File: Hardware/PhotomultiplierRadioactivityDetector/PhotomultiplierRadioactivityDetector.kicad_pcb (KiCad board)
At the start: 2 copper layers, 100 x 100 mm, 83 parts, among them J1 Conn_01x04, J10 Conn_01x01_Male, J11 Conn_01x01_Male, J12 Conn_01x01_Male, J13 Conn_01x01_Male, J14 Conn_01x01_Male, J2 Conn_02x05_Counter_Clockwise, J3 Conn_01x01_Male, J4 Conn_01x01_Male, J5 Conn_01x01_Male, J6 Conn_01x01_Male, J7 Conn_01x01_Male, J8 Conn_01x01_Male, J9 Conn_01x01_Male, Q1 2N7002, Q2 Q_NPN_BEC, U1 Opamp_Dual_Generic, U2 MCP3425A0T-ECH, U3 MCP3425A0T-ECH, U4 STM8S003F3P

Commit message: initial version rework
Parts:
- removed RV1: R_POT_TRIM, Potentiometer_THT:Potentiometer_Bourns_3296W_Vertical
- added D6: 1n148, Diode_SMD:D_MiniMELF, F.Cu at (87.9, 181.0)
- added D7: red, LED_SMD:LED_0805_2012Metric, F.Cu at (111.7, 156.4)
- added J15: Conn_01x02_Female, Connector_PinHeader_2.54mm:PinHeader_2x01_P2.54mm_Vertical, F.Cu at (116.0, 186.0)
- added R31: 2k2, Resistor_SMD:R_0805_2012Metric_Pad1.15x1.40mm_HandSolder, F.Cu at (96.6, 161.8)
- added R32: 510R, Resistor_SMD:R_0805_2012Metric_Pad1.15x1.40mm_HandSolder, F.Cu at (91.9, 162.1)
- added R33: 510R, Resistor_SMD:R_0805_2012Metric_Pad1.15x1.40mm_HandSolder, F.Cu at (87.1, 162.1)
- added R34: 510R, Resistor_SMD:R_0805_2012Metric_Pad1.15x1.40mm_HandSolder, F.Cu at (93.5, 158.8)
- added R35: 10k, Resistor_SMD:R_0805_2012Metric_Pad1.15x1.40mm_HandSolder, F.Cu at (40.0, 173.8)
- added R36: 10k, Resistor_SMD:R_0805_2012Metric_Pad1.15x1.40mm_HandSolder, F.Cu at (44.8, 170.9)
- added Rel1: RSM850B-6112-85-1005, Relay_THT:Relay_DPDT_Omron_G6K-2P-Y, F.Cu at (86.4, 169.8)
- C1, C6, C9: value 100n -> 10n
- C10, C11, C12, C13, C14, C15, C16, C17, C18, C19, C20, C21: value C -> 10n/3kV
- C2: value 10u -> 10n; footprint Capacitor_Tantalum_SMD:CP_EIA-3528-21_Kemet-B -> Capacitor_SMD:C_0805_2012Metric_Pad1.15x1.40mm_HandSolder
- C7: value 10n -> 680n
- C8: value 680n -> 100n
- D2: value yellow -> 1n148; footprint LED_SMD:LED_0805_2012Metric -> Diode_SMD:D_MiniMELF
- D3: value 0R resistor -> yellow; footprint Diode_SMD:D_MiniMELF -> LED_SMD:LED_0805_2012Metric
- D4: value green -> 0R resistor; footprint LED_SMD:LED_0805_2012Metric -> Diode_SMD:D_MiniMELF
- D5: value red -> green
- Q2: footprint Package_TO_SOT_SMD:SOT-323_SC-70_Handsoldering -> Package_TO_SOT_SMD:SOT-323_SC-70
- R10: value 2k2 -> 1k
- R11: value 2k2 -> 10k
- R12, R13: value 510R -> 0R
- R14: value 510R -> 2k2
- R15, R16, R17, R18, R19, R20, R22, R23, R24, R25, R26, R27, R28, R29, R30: value R -> 150k
- R2, R7: value 0R -> 10k
- R3: value 27k -> 10k
- R4, R5, R8, R9: value 1k -> 10k
- R6: value 0R -> 100R
- U1: value Opamp_Dual_Generic -> TL074; footprint Package_SO:SOIC-8_3.9x4.9mm_P1.27mm -> Package_SO:SOIC-14_3.9x8.7mm_P1.27mm
- U2: value MCP3425A0T-ECH -> STM8S003F3P; footprint Package_TO_SOT_SMD:SOT-23-6_Handsoldering -> Package_SO:TSSOP-20_4.4x6.5mm_P0.65mm
- U4: value STM8S003F3P -> TL074; footprint Package_SO:TSSOP-20_4.4x6.5mm_P0.65mm -> Package_SO:SOIC-14_3.9x8.7mm_P1.27mm
- moved J1 76.7 mm to (111.7, 144.9)
- moved R21 71.1 mm to (95.0, 115.0)
- moved J11 69.9 mm to (93.0, 95.0)
- moved R14 68.5 mm to (116.4, 144.1)
- moved R24 64.2 mm to (90.0, 120.0)
- moved TP2 64.2 mm to (120.3, 150.1)
- moved R26 63.2 mm to (100.0, 130.0)
- moved TP4 61.1 mm to (120.0, 153.2)
- moved J3 59.8 mm to (37.0, 95.0)
- moved C6 58.3 mm to (116.4, 147.1)
- moved D3 57.7 mm to (116.3, 153.0)
- moved C2 57.6 mm to (101.8, 169.1)
- moved J2 57.4 mm to (98.3, 144.9)
- moved C7 56.4 mm to (116.4, 150.0)
- moved R25 54.9 mm to (85.0, 110.0)
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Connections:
- C1 pad 1: ANODE_OUTPUT -> Net-(C1-Pad1)
- C2 pad 1: VCC_5V -> ANODE_OUTPUT
- C2 pad 2: ANODE_OUTPUT -> Net-(C2-Pad2)
- C6 pad 2: VCC_5V -> /DataProcessing/RST
- C7 pad 2: /DataAcquisition/RST -> Net-(C7-Pad2)
- C8 pad 2: Net-(C8-Pad2) -> /DataProcessing/VCC_PROG
- C9 pad 2: /DataAcquisition/VCC_PROG -> Net-(C9-Pad2)
- D2 pad 1: ANODE_OUTPUT -> +9V
- D3 pad 1: /DataAcquisition/VCC_PROG -> ANODE_OUTPUT
- D3 pad 2: VCC_5V -> Net-(D3-Pad2)
- D4 pad 1: ANODE_OUTPUT -> /DataProcessing/VCC_PROG
- D4 pad 2: Net-(D4-Pad2) -> VCC_5V
- J1 pad 2: /DataAcquisition/RX -> /DataProcessing/RX
- J1 pad 3: /DataAcquisition/TX -> /DataProcessing/TX
- J2 pad 1: /DataAcquisition/RST -> /DataProcessing/RST
- J2 pad 2: /DataAcquisition/SWIM -> /DataProcessing/SWIM
- J2 pad 5: /DataAcquisition/VCC_PROG -> /DataProcessing/VCC_PROG
- Q2 pad 1: Net-(D1-Pad1) -> Net-(C2-Pad2)
- Q2 pad 2: (no net) -> ANODE_OUTPUT
- Q2 pad 3: Net-(C1-Pad2) -> Net-(D2-Pad2)
- R1 pad 1: /DataAcquisition/RST_PEAK -> Net-(Q1-Pad1)
- R1 pad 2: Net-(Q1-Pad1) -> (no net)
- R10 pad 1: /DataAcquisition/SCL -> (no net)
- R10 pad 2: VCC_5V -> Net-(C2-Pad2)
- R11 pad 1: /DataAcquisition/SDA -> Net-(C2-Pad2)
- R11 pad 2: VCC_5V -> ANODE_OUTPUT
- R12 pad 1: Net-(D2-Pad2) -> Net-(R12-Pad1)
- R13 pad 1: Net-(D4-Pad2) -> Net-(R13-Pad1)
- R13 pad 2: Net-(R13-Pad2) -> ANODE_OUTPUT
- R14 pad 1: Net-(D5-Pad2) -> /DataProcessing/SCL
- R14 pad 2: Net-(R14-Pad2) -> VCC_5V
- R2 pad 1: Net-(R2-Pad1) -> Net-(D1-Pad2)
- R2 pad 2: analog_output -> Net-(R2-Pad2)
- R3 pad 1: ANODE_OUTPUT -> Net-(D1-Pad1)
- R3 pad 2: Net-(R2-Pad1) -> Net-(R2-Pad2)
- R4 pad 2: Net-(R4-Pad2) -> Net-(C9-Pad2)
- R5 pad 1: Net-(R5-Pad1) -> Net-(C9-Pad2)
- R6 pad 1: Net-(R6-Pad1) -> Net-(C1-Pad1)
- R6 pad 2: Net-(R2-Pad1) -> ANODE_OUTPUT
- R7 pad 1: Net-(R7-Pad1) -> Net-(Q1-Pad1)
- R8 pad 1: Net-(R8-Pad1) -> (no net)
- R9 pad 2: /DataAcquisition/INT0 -> Net-(R35-Pad1)
- U1 pad 1: Net-(D1-Pad2) -> (no net)
- U1 pad 2: Net-(D1-Pad1) -> (no net)
- U1 pad 3: analog_output -> (no net)
- U1 pad 4: ANODE_OUTPUT -> (no net)
- U1 pad 5: analog_output -> (no net)
- U1 pad 6: Net-(R8-Pad2) -> (no net)
- U1 pad 7: /DataAcquisition/INT0 -> (no net)
- U1 pad 8: VCC_5V -> (no net)
- U2 pad 1: Net-(R6-Pad1) -> (no net)
- U2 pad 2: ANODE_OUTPUT -> /DataProcessing/TX
- U2 pad 3: /DataAcquisition/SCL -> /DataProcessing/RX
- U2 pad 4: /DataAcquisition/SDA -> /DataProcessing/RST
- U2 pad 5: VCC_5V -> (no net)
- U2 pad 6: Net-(R7-Pad1) -> Net-(R32-Pad2)
- U3 pad 1: Net-(C1-Pad2) -> Net-(R12-Pad1)
- U3 pad 3: /DataAcquisition/SCL -> (no net)
- U3 pad 4: /DataAcquisition/SDA -> (no net)
- U3 pad 6: ANODE_OUTPUT -> Net-(R13-Pad1)
- U4 pad 1: /DataAcquisition/INT0 -> Net-(D1-Pad1)
- U4 pad 10: Net-(TP1-Pad1) -> Net-(C9-Pad2)
- U4 pad 11: /DataAcquisition/SDA -> ANODE_OUTPUT
- U4 pad 12: /DataAcquisition/SCL -> Net-(C9-Pad2)
- U4 pad 13: Net-(TP2-Pad1) -> Net-(R35-Pad2)
- U4 pad 14: Net-(TP3-Pad1) -> Net-(R36-Pad2)
- U4 pad 2: /DataAcquisition/TX -> Net-(D1-Pad2)
- U4 pad 3: /DataAcquisition/RX -> (no net)
- U4 pad 4: /DataAcquisition/RST -> VCC_5V
- U4 pad 5: /DataAcquisition/RST_PEAK -> Net-(C1-Pad2)
- U4 pad 6: Net-(R12-Pad2) -> Net-(R2-Pad2)
- U4 pad 7: ANODE_OUTPUT -> Net-(R2-Pad2)
- U4 pad 8: Net-(C8-Pad2) -> Net-(R35-Pad1)
- U4 pad 9: /DataAcquisition/VCC_PROG -> Net-(R8-Pad2)
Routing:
- added copper zone on F.Cu, net (none)
- added copper zone on F.Cu, net VCC_5V

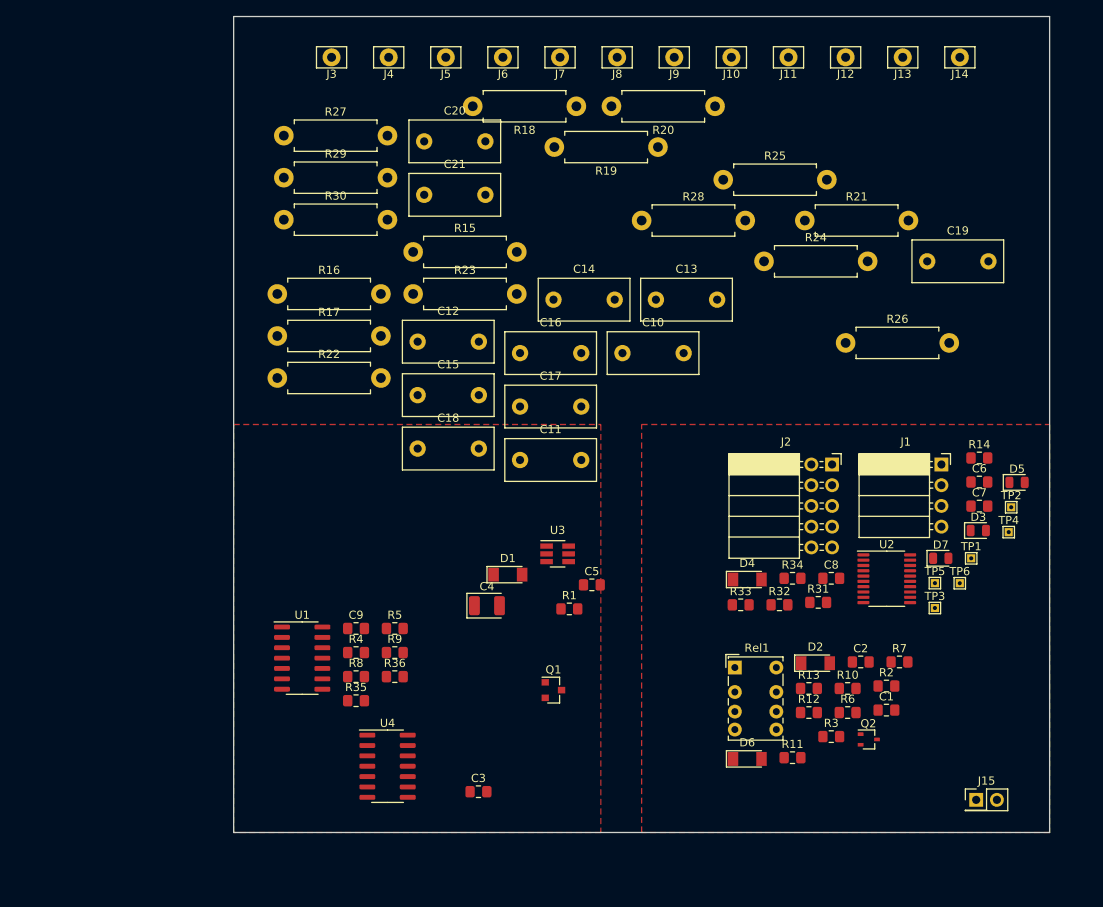
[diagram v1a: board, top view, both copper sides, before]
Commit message: draft of hw power supply
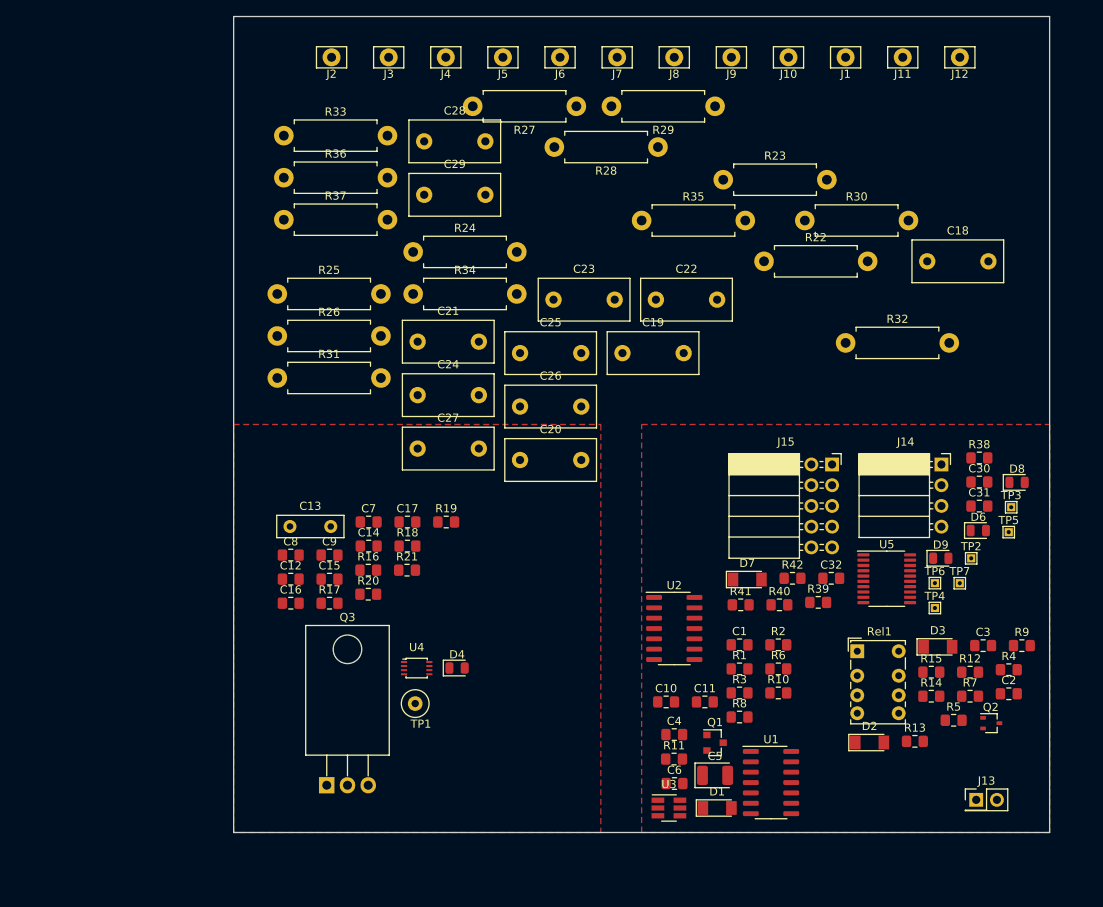
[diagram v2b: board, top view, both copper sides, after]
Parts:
- removed the U1 at (33.4, 168.6)
- added C10: 100n, Capacitor_SMD:C_0805_2012Metric_Pad1.15x1.40mm_HandSolder, F.Cu at (78.0, 174.0)
- added C11: 100n, Capacitor_SMD:C_0805_2012Metric_Pad1.15x1.40mm_HandSolder, F.Cu at (82.8, 174.0)
- added C12: 100n, Capacitor_SMD:C_0805_2012Metric_Pad1.15x1.40mm_HandSolder, F.Cu at (32.0, 158.9)
- added C13: C, Capacitor_THT:C_Disc_D8.0mm_W2.5mm_P5.00mm, F.Cu at (31.9, 152.5)
- added C14: 10n, Capacitor_SMD:C_0805_2012Metric_Pad1.15x1.40mm_HandSolder, F.Cu at (41.5, 154.9)
- added C15: 10n, Capacitor_SMD:C_0805_2012Metric_Pad1.15x1.40mm_HandSolder, F.Cu at (36.8, 158.9)
- added C16: 10n, Capacitor_SMD:C_0805_2012Metric_Pad1.15x1.40mm_HandSolder, F.Cu at (32.0, 161.9)
- added C17: 10n, Capacitor_SMD:C_0805_2012Metric_Pad1.15x1.40mm_HandSolder, F.Cu at (46.3, 151.9)
- added C7: 100n, Capacitor_SMD:C_0805_2012Metric_Pad1.15x1.40mm_HandSolder, F.Cu at (41.5, 151.9)
- added C8: 10n, Capacitor_SMD:C_0805_2012Metric_Pad1.15x1.40mm_HandSolder, F.Cu at (32.0, 156.0)
- added C9: 10n, Capacitor_SMD:C_0805_2012Metric_Pad1.15x1.40mm_HandSolder, F.Cu at (36.8, 156.0)
- added D4: red, LED_SMD:LED_0805_2012Metric, F.Cu at (52.4, 169.8)
- added Q3: Q_NMOS_GDS, Package_TO_SOT_THT:TO-220-3_Horizontal_TabDown, F.Cu at (36.4, 184.2)
- added R16: 10k, Resistor_SMD:R_0805_2012Metric_Pad1.15x1.40mm_HandSolder, F.Cu at (41.5, 157.8)
- added R17: 10k, Resistor_SMD:R_0805_2012Metric_Pad1.15x1.40mm_HandSolder, F.Cu at (36.8, 161.9)
- added R18: 10k, Resistor_SMD:R_0805_2012Metric_Pad1.15x1.40mm_HandSolder, F.Cu at (46.3, 154.9)
- added R19: 10k, Resistor_SMD:R_0805_2012Metric_Pad1.15x1.40mm_HandSolder, F.Cu at (51.0, 151.9)
- added R20: 10k, Resistor_SMD:R_0805_2012Metric_Pad1.15x1.40mm_HandSolder, F.Cu at (41.5, 160.8)
- added R21: 10k, Resistor_SMD:R_0805_2012Metric_Pad1.15x1.40mm_HandSolder, F.Cu at (46.2, 157.8)
- added TP1: TestPoint, TestPoint:TestPoint_Loop_D2.60mm_Drill0.9mm_Beaded, F.Cu at (47.2, 174.2)
- added U2: TL074, Package_SO:SOIC-14_3.9x8.7mm_P1.27mm, F.Cu at (79.0, 165.0)
- added U4: LM3488, Package_SO:VSSOP-8_2.4x2.1mm_P0.5mm, F.Cu at (47.4, 169.8)
- moved C1 47.0 mm to (87.0, 167.0)
- moved R1 47.0 mm to (87.0, 169.9)
- moved R10 47.0 mm to (91.8, 172.9)
- moved R2 47.0 mm to (91.8, 167.0)
- moved R3 47.0 mm to (87.0, 172.9)
- moved R6 47.0 mm to (91.8, 169.9)
- moved R8 47.0 mm to (87.0, 175.8)
- moved U1 47.0 mm to (90.9, 183.9)
- moved D1 38.4 mm to (84.2, 187.0)
- moved C5 34.8 mm to (84.0, 183.0)
- moved U3 34.0 mm to (78.3, 187.0)
- moved C6 26.4 mm to (79.0, 184.0)
- moved C4 25.0 mm to (79.0, 178.0)
- moved R11 22.4 mm to (79.0, 181.0)
- moved Q1 20.8 mm to (84.0, 179.0)
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- renumbered C9 to C1, C19 to C18, C10 to C19, C1 to C2, C11 to C20, C12 to C21, C13 to C22, C14 to C23, C15 to C24, C16 to C25, C17 to C26, C18 to C27, C20 to C28, C21 to C29, C2 to C3, C6 to C30, C7 to C31, C8 to C32, C3 to C4, C4 to C5, C5 to C6, D6 to D2, D2 to D3, D3 to D6, D4 to D7, D5 to D8, D7 to D9, J12 to J1, J11 to J10, J13 to J11, J14 to J12, J15 to J13, J1 to J14, J2 to J15, J3 to J2, J4 to J3, J5 to J4, J6 to J5, J7 to J6, J8 to J7, J9 to J8, J10 to J9, R4 to R1, R36 to R10, R1 to R11, R10 to R12, R11 to R13, R12 to R14, R13 to R15, R5 to R2, R24 to R22, R25 to R23, R15 to R24, R16 to R25, R17 to R26, R18 to R27, R19 to R28, R20 to R29, R8 to R3, R21 to R30, R22 to R31, R26 to R32, R27 to R33, R23 to R34, R28 to R35, R29 to R36, R30 to R37, R14 to R38, R31 to R39, R2 to R4, R32 to R40, R33 to R41, R34 to R42, R3 to R5, R9 to R6, R6 to R7, R35 to R8, R7 to R9, TP1 to TP2, TP2 to TP3, TP3 to TP4, TP4 to TP5, TP5 to TP6, TP6 to TP7, U4 to U1, U2 to U5
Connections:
- U1 pad 11: ANODE_OUTPUT -> (no net)
- U1 pad 4: VCC_5V -> (no net)
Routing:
- added copper zone on F.Cu, net VCC
- removed copper zone on F.Cu, net (none)

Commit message: add element/footprint for photomultiplier
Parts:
- removed J1, J10, J11, J12, J2, J3, J4, J5, J6, J7, J8, J9: Conn_01x01_Male, Connector_Pin:Pin_D1.1mm_L10.2mm_W3.5mm_Flat
- added EL1: Photomultiplier, PhotomultiplierRadioactivityDetector:PhotomultiplierGeneric, F.Cu at (98.0, 110.0)
- C14, C15, C16, C17: footprint Capacitor_SMD:C_0805_2012Metric_Pad1.15x1.40mm_HandSolder -> Capacitor_THT:C_Disc_D11.0mm_W5.0mm_P7.50mm
- R20, R21: footprint Resistor_SMD:R_0805_2012Metric_Pad1.15x1.40mm_HandSolder -> Resistor_THT:R_Axial_DIN0411_L9.9mm_D3.6mm_P12.70mm_Horizontal

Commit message: draft of amplifier
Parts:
- added C33: 10n/3kV, Capacitor_THT:C_Disc_D11.0mm_W5.0mm_P7.50mm, F.Cu at (68.8, 129.6)
- added C34: 10n/3kV, Capacitor_THT:C_Disc_D11.0mm_W5.0mm_P7.50mm, F.Cu at (68.8, 136.1)
- added C35: 2p2, Capacitor_SMD:C_0805_2012Metric_Pad1.15x1.40mm_HandSolder, F.Cu at (85.8, 167.4)
- added C36: 2p2, Capacitor_SMD:C_0805_2012Metric_Pad1.15x1.40mm_HandSolder, F.Cu at (82.9, 162.7)
- added C37: 1n, Capacitor_SMD:C_0805_2012Metric_Pad1.15x1.40mm_HandSolder, F.Cu at (74.4, 154.2)
- added C38: 1n, Capacitor_SMD:C_0805_2012Metric_Pad1.15x1.40mm_HandSolder, F.Cu at (67.1, 146.4)
- added C39: 100n, Capacitor_SMD:C_0805_2012Metric_Pad1.15x1.40mm_HandSolder, F.Cu at (77.3, 154.2)
- added C40: 100n, Capacitor_SMD:C_0805_2012Metric_Pad1.15x1.40mm_HandSolder, F.Cu at (82.9, 157.9)
- added C41: 4p7+2p2, Capacitor_SMD:C_0805_2012Metric_Pad1.15x1.40mm_HandSolder, F.Cu at (85.8, 162.7)
- added C42: 4p7+2p2, Capacitor_SMD:C_0805_2012Metric_Pad1.15x1.40mm_HandSolder, F.Cu at (72.7, 149.5)
- added C44: 100n, Capacitor_SMD:C_0805_2012Metric_Pad1.15x1.40mm_HandSolder, F.Cu at (67.1, 141.7)
- added D10: 1n148, Diode_SMD:D_MELF, F.Cu at (81.0, 151.7)
- added D11: 1n148, Diode_SMD:D_MELF, F.Cu at (70.7, 143.2)
- added D12: 1n148, Diode_SMD:D_MELF, F.Cu at (85.2, 151.7)
- added D13: 1n148, Diode_SMD:D_MELF, F.Cu at (75.0, 143.2)
- added D5: D, Diode_SMD:D_MELF, F.Cu at (58.6, 146.0)
- added R43: 10G, Resistor_SMD:R_0805_2012Metric_Pad1.15x1.40mm_HandSolder, F.Cu at (85.8, 172.2)
- added R44: 10G, Resistor_SMD:R_0805_2012Metric_Pad1.15x1.40mm_HandSolder, F.Cu at (71.5, 155.9)
- added R45: 10k, Resistor_SMD:R_0805_2012Metric_Pad1.15x1.40mm_HandSolder, F.Cu at (77.0, 163.8)
- added R46: 10k, Resistor_SMD:R_0805_2012Metric_Pad1.15x1.40mm_HandSolder, F.Cu at (80.0, 168.5)
- added R47: 10k, Resistor_SMD:R_0805_2012Metric_Pad1.15x1.40mm_HandSolder, F.Cu at (68.5, 155.9)
- added R48: 10k, Resistor_SMD:R_0805_2012Metric_Pad1.15x1.40mm_HandSolder, F.Cu at (82.9, 172.2)
- added R49: 10k, Resistor_SMD:R_0805_2012Metric_Pad1.15x1.40mm_HandSolder, F.Cu at (74.0, 160.7)
- added R50: 10k, Resistor_SMD:R_0805_2012Metric_Pad1.15x1.40mm_HandSolder, F.Cu at (71.1, 160.7)
- added R51: 10M, Resistor_SMD:R_0805_2012Metric_Pad1.15x1.40mm_HandSolder, F.Cu at (77.0, 168.5)
- added R52: 10M, Resistor_SMD:R_0805_2012Metric_Pad1.15x1.40mm_HandSolder, F.Cu at (74.0, 165.4)
- C1: value 10n -> 100n
- R10, R8: value 10k -> 0R
- moved R32 69.4 mm to (30.6, 131.2)
- moved C22 49.4 mm to (31.1, 143.6)
- moved R8 31.9 mm to (66.8, 151.2), turned to 270 degrees
- moved C20 29.9 mm to (31.1, 137.1)
- moved C29 29.1 mm to (56.2, 139.8)
- moved R3 27.8 mm to (69.7, 151.2), turned to 270 degrees
- moved R35 27.8 mm to (47.2, 115.8)
- moved C26 27.2 mm to (77.0, 116.5)
- moved R1 23.4 mm to (75.6, 149.5), turned to 270 degrees
- moved R31 23.2 mm to (33.4, 111.3)
- moved R24 23.2 mm to (50.0, 95.8)
- moved R25 23.2 mm to (33.4, 101.0)
- moved R26 23.2 mm to (33.4, 106.2)
- moved R33 22.9 mm to (47.2, 120.9)
- moved U2 21.7 mm to (82.2, 143.5), turned to 270 degrees
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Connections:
- C1 pad 1: ANODE_OUTPUT -> Net-(C1-Pad1)
- C1 pad 2: Net-(C1-Pad2) -> GND
- C10 pad 2: ANODE_OUTPUT -> GND
- C11 pad 2: ANODE_OUTPUT -> GND
- C12 pad 2: ANODE_OUTPUT -> GND
- C13 pad 2: ANODE_OUTPUT -> GND
- C14 pad 1: ANODE_OUTPUT -> GND
- C15 pad 1: ANODE_OUTPUT -> GND
- C16 pad 1: ANODE_OUTPUT -> GND
- C17 pad 1: ANODE_OUTPUT -> GND
- C18 pad 1: Net-(C18-Pad1) -> GND
- C18 pad 2: ANODE_OUTPUT -> Net-(C18-Pad2)
- C20 pad 2: ANODE_OUTPUT -> DYNOE_OUTPUT
- C21 pad 2: ANODE_OUTPUT -> Net-(C18-Pad2)
- C22 pad 2: ANODE_OUTPUT -> Net-(C21-Pad1)
- C23 pad 2: ANODE_OUTPUT -> Net-(C22-Pad1)
- C24 pad 2: ANODE_OUTPUT -> Net-(C23-Pad1)
- C25 pad 1: Net-(C25-Pad1) -> GND
- C25 pad 2: ANODE_OUTPUT -> Net-(C24-Pad1)
- C26 pad 2: ANODE_OUTPUT -> Net-(C18-Pad2)
- C27 pad 2: ANODE_OUTPUT -> Net-(C26-Pad1)
- C28 pad 2: Net-(C28-Pad2) -> Net-(C27-Pad1)
- C29 pad 1: (no net) -> Net-(C29-Pad1)
- C29 pad 2: Net-(C29-Pad2) -> Net-(C28-Pad1)
- C3 pad 1: ANODE_OUTPUT -> GND
- C30 pad 1: ANODE_OUTPUT -> GND
- C31 pad 1: ANODE_OUTPUT -> GND
- C32 pad 1: ANODE_OUTPUT -> GND
- C4 pad 1: ANODE_OUTPUT -> Net-(C4-Pad1)
- C4 pad 2: VCC_5V -> GND
- C5 pad 2: ANODE_OUTPUT -> GND
- C6 pad 1: ANODE_OUTPUT -> GND
- C7 pad 1: ANODE_OUTPUT -> GND
- C8 pad 1: ANODE_OUTPUT -> GND
- C9 pad 1: ANODE_OUTPUT -> GND
- D6 pad 1: ANODE_OUTPUT -> GND
- D8 pad 1: ANODE_OUTPUT -> GND
- D9 pad 1: ANODE_OUTPUT -> GND
- EL1 pad 1: Net-(C18-Pad1) -> Net-(C18-Pad2)
- EL1 pad 10: Net-(EL1-Pad10) -> Net-(C33-Pad1)
- EL1 pad 11: Net-(C28-Pad1) -> Net-(EL1-Pad11)
- EL1 pad 12: Net-(EL1-Pad12) -> GND
- EL1 pad 2: Net-(C19-Pad1) -> Net-(C26-Pad1)
- EL1 pad 3: Net-(C20-Pad1) -> Net-(C21-Pad1)
- EL1 pad 4: Net-(C21-Pad1) -> Net-(C27-Pad1)
- EL1 pad 6: Net-(C23-Pad1) -> Net-(C28-Pad1)
- EL1 pad 7: Net-(C24-Pad1) -> Net-(C23-Pad1)
- EL1 pad 8: Net-(C25-Pad1) -> Net-(C29-Pad1)
- EL1 pad 9: Net-(C26-Pad1) -> Net-(C24-Pad1)
- J13 pad 1: ANODE_OUTPUT -> GND
- J14 pad 4: ANODE_OUTPUT -> GND
- J15 pad 3: ANODE_OUTPUT -> GND
- Q1 pad 2: ANODE_OUTPUT -> GND
- Q2 pad 2: ANODE_OUTPUT -> GND
- R1 pad 1: VCC_5V -> VCC
- R1 pad 2: Net-(C1-Pad2) -> Net-(C1-Pad1)
- R10 pad 1: Net-(R10-Pad1) -> DYNOE_OUTPUT
- R10 pad 2: Net-(R10-Pad2) -> Net-(C36-Pad2)
- R13 pad 2: ANODE_OUTPUT -> GND
- R15 pad 2: ANODE_OUTPUT -> GND
- R16 pad 2: ANODE_OUTPUT -> GND
- R18 pad 2: ANODE_OUTPUT -> GND
- R19 pad 2: ANODE_OUTPUT -> GND
- R2 pad 1: Net-(C1-Pad2) -> Net-(C1-Pad1)
- R2 pad 2: ANODE_OUTPUT -> GND
- R21 pad 2: ANODE_OUTPUT -> GND
- R22 pad 2: Net-(C18-Pad1) -> Net-(C18-Pad2)
- R23 pad 1: Net-(C19-Pad1) -> Net-(C26-Pad1)
- R23 pad 2: Net-(C18-Pad1) -> Net-(C18-Pad2)
- R24 pad 1: Net-(C20-Pad1) -> Net-(C21-Pad1)
- R24 pad 2: Net-(C19-Pad1) -> Net-(C26-Pad1)
- R25 pad 1: Net-(C21-Pad1) -> Net-(C27-Pad1)
- R25 pad 2: Net-(C20-Pad1) -> Net-(C21-Pad1)
- R26 pad 2: Net-(C21-Pad1) -> Net-(C27-Pad1)
- R27 pad 1: Net-(C23-Pad1) -> Net-(C28-Pad1)
- R28 pad 1: Net-(C24-Pad1) -> Net-(C23-Pad1)
- R28 pad 2: Net-(C23-Pad1) -> Net-(C28-Pad1)
- R29 pad 1: Net-(C25-Pad1) -> Net-(C29-Pad1)
- R29 pad 2: Net-(C24-Pad1) -> Net-(C23-Pad1)
- R3 pad 1: (no net) -> VCC
- R3 pad 2: Net-(R3-Pad2) -> Net-(C4-Pad1)
- R30 pad 1: Net-(C26-Pad1) -> Net-(C24-Pad1)
- R30 pad 2: Net-(C25-Pad1) -> Net-(C29-Pad1)
- R31 pad 1: Net-(C27-Pad1) -> Net-(C33-Pad1)
- R31 pad 2: Net-(C26-Pad1) -> Net-(C24-Pad1)
- R32 pad 1: Net-(C29-Pad2) -> ANODE_OUTPUT
- R32 pad 2: Net-(EL1-Pad10) -> GND
- R33 pad 1: Net-(C27-Pad1) -> DYNOE_OUTPUT
- R33 pad 2: Net-(C29-Pad2) -> GND
- R34 pad 1: Net-(C28-Pad2) -> Net-(C18-Pad2)
- R34 pad 2: Net-(C27-Pad1) -> Net-(C19-Pad1)
- R35 pad 1: Net-(C28-Pad1) -> Net-(C26-Pad1)
- R35 pad 2: Net-(C28-Pad2) -> Net-(C20-Pad1)
- R36 pad 1: ANODE_OUTPUT -> Net-(EL1-Pad11)
- R36 pad 2: Net-(C28-Pad1) -> Net-(C33-Pad1)
- R37 pad 1: ANODE_OUTPUT -> GND
- R37 pad 2: Net-(EL1-Pad12) -> Net-(EL1-Pad11)
- R6 pad 1: Net-(R3-Pad2) -> Net-(C4-Pad1)
- R6 pad 2: Net-(R6-Pad2) -> GND
- R7 pad 2: ANODE_OUTPUT -> GND
- R8 pad 1: Net-(R6-Pad2) -> ANODE_OUTPUT
- R8 pad 2: Net-(R10-Pad1) -> Net-(C35-Pad2)
- R9 pad 2: ANODE_OUTPUT -> GND
- U1 pad 10: Net-(C1-Pad2) -> Net-(C4-Pad1)
- U1 pad 11: (no net) -> GND
- U1 pad 12: Net-(C1-Pad2) -> Net-(C40-Pad1)
- U1 pad 13: Net-(R10-Pad1) -> Net-(C42-Pad2)
- U1 pad 14: Net-(R10-Pad2) -> Net-(C42-Pad1)
- U1 pad 4: (no net) -> Net-(C44-Pad1)
- U1 pad 8: Net-(R6-Pad2) -> Net-(C36-Pad1)
- U1 pad 9: Net-(R3-Pad2) -> DYNOE_OUTPUT
- U2 pad 1: (no net) -> Net-(C35-Pad1)
- U2 pad 11: ANODE_OUTPUT -> (no net)
- U2 pad 2: (no net) -> ANODE_OUTPUT
- U2 pad 3: (no net) -> Net-(C1-Pad1)
- U2 pad 4: VCC_5V -> (no net)
- U2 pad 5: (no net) -> Net-(C39-Pad1)
- U2 pad 6: (no net) -> Net-(C41-Pad2)
- U2 pad 7: (no net) -> Net-(C41-Pad1)
- U3 pad 2: ANODE_OUTPUT -> GND
- U4 pad 4: ANODE_OUTPUT -> GND
- U5 pad 7: ANODE_OUTPUT -> GND
